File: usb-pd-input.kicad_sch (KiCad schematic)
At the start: 8 parts, among them J1 USB-C

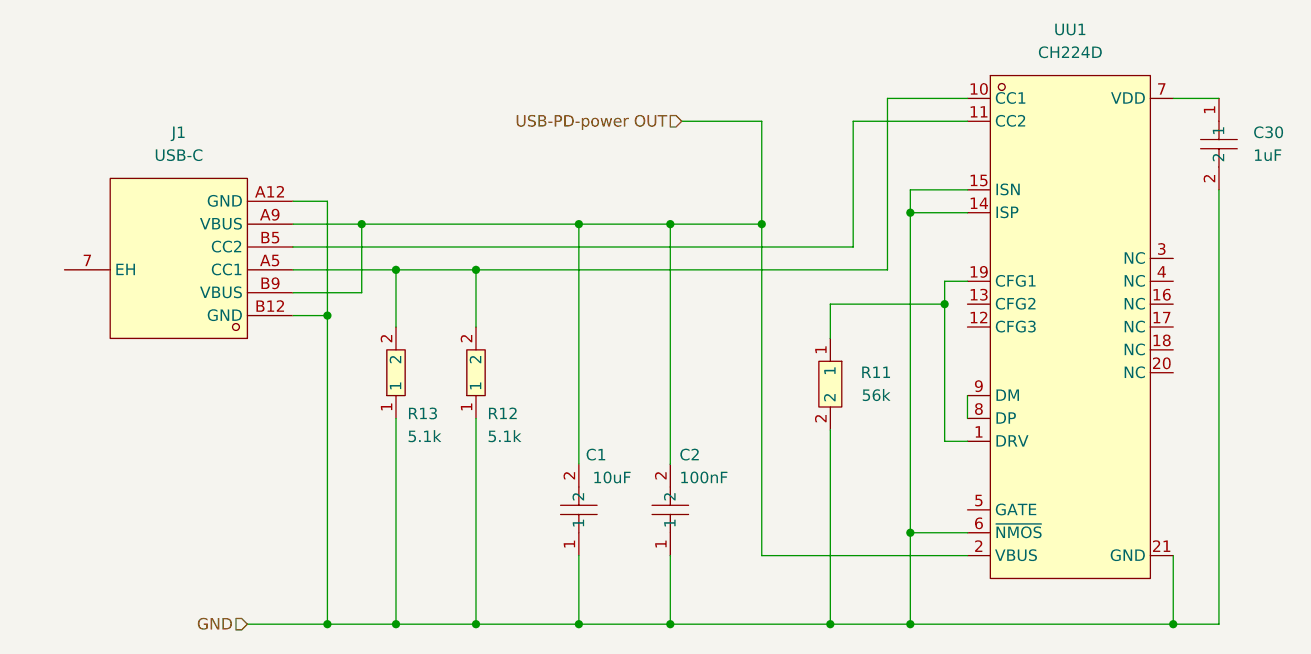
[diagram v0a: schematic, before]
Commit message: KiCad回路図とPCBレイアウトの更新
- DC-DC変換段、リニアレギュレーション段の回路図を更新
- USB-PD入力段と出力段の回路図を更新
- PCBレイアウトにコンポーネントを配置
- シンボルライブラリを更新

Co-Authored-By: Claude Opus 4.5 <noreply@anthropic.com>
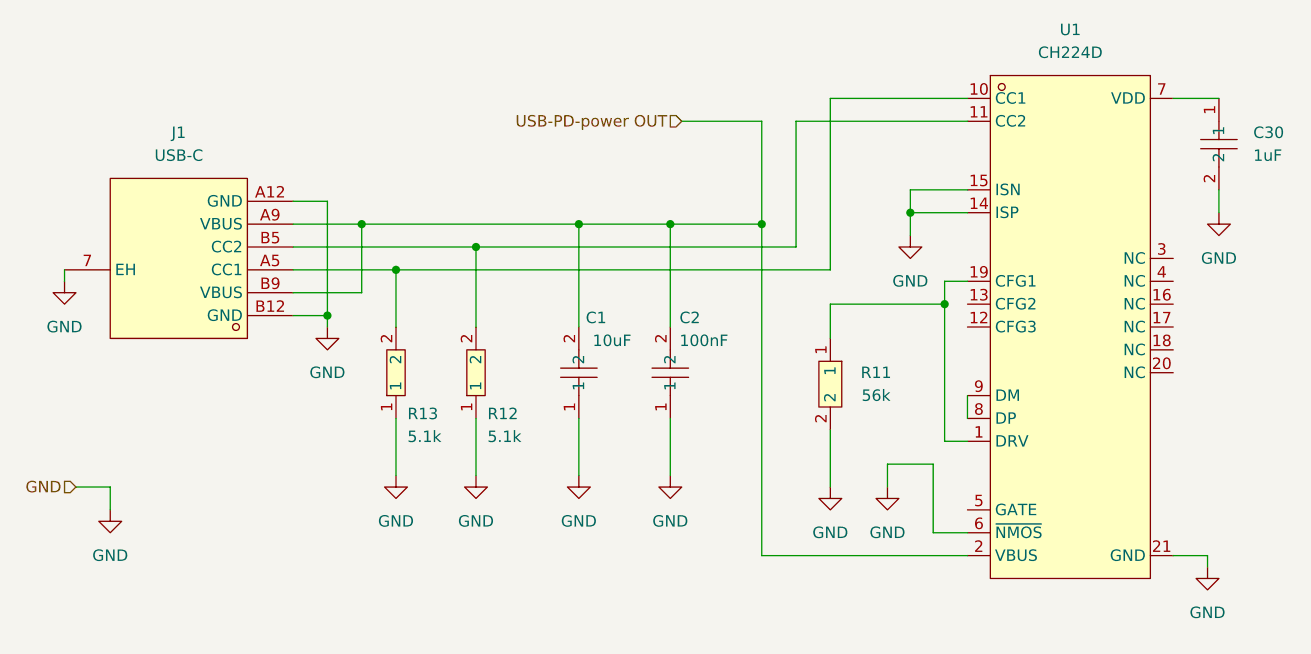
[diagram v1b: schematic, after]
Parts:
- C1: footprint easyeda2kicad:C1206 -> zudo-pd:C1206
- C2: footprint easyeda2kicad:C0805 -> zudo-pd:C0805
- C30: footprint easyeda2kicad:C0603 -> zudo-pd:C0603
- J1: footprint easyeda2kicad:TYPE-C-SMD_TYPE-C-6P -> zudo-pd:TYPE-C-SMD_TYPE-C-6P
- R11, R12, R13: footprint easyeda2kicad:R0603 -> zudo-pd:R0603
- U1: renamed from UU1; footprint easyeda2kicad:QFN-20_L3.0-W3.0-P0.40-BL-EP1.7 -> zudo-pd:QFN-20_L3.0-W3.0-P0.40-BL-EP1.7
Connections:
- net GND: now also J1.7 (EH)
- net at J1.A5 (CC1), R13.2, U1.10 (CC1): no longer R12.2
- net at J1.B5 (CC2), U1.11 (CC2): now also R12.2
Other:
- moved on the sheet: C1, C2
